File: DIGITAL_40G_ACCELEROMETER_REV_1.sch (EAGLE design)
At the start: 26 parts, among them IC1 ADIS16500AMLZ, IC2 LTC6820IUD#PBF, IC3 LDL1117S33R, T1 782482_33VC

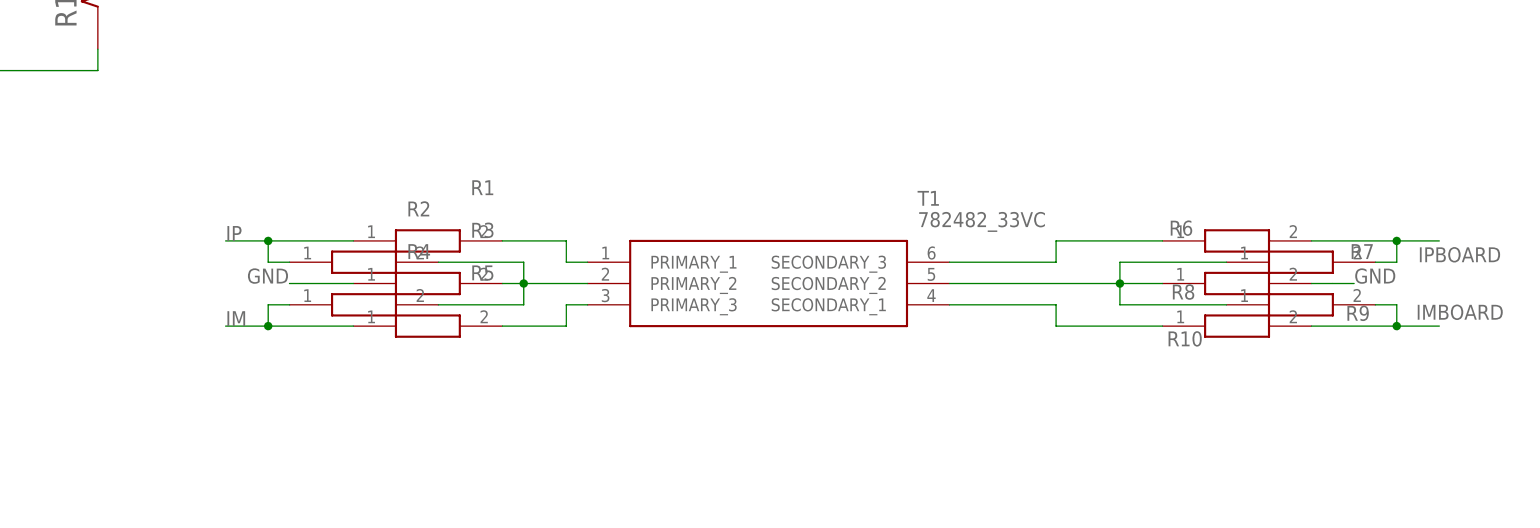
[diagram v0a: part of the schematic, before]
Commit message: Completed First Draft of Digital 40G Board Layout
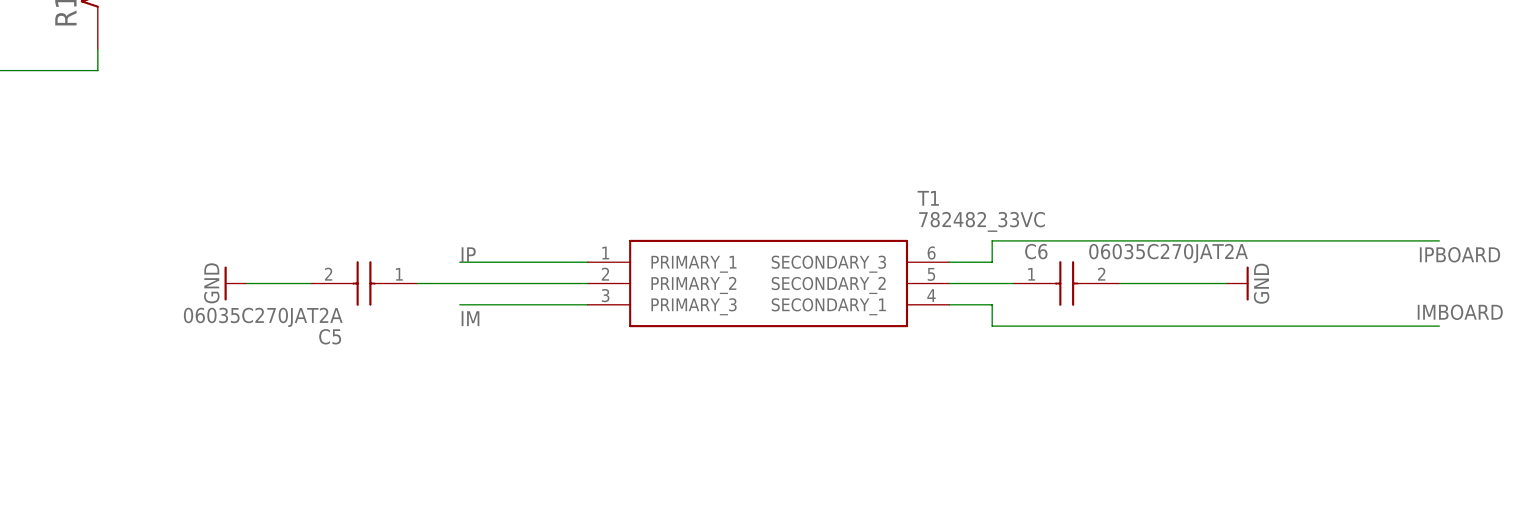
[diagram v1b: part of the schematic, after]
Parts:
- removed R1, R10, R2, R3, R4, R5, R6, R7, R8, R9: CRG0402ZR, CRG0402ZR:CRG0402ZR
- added C5, C6: 06035C270JAT2A, SamacSys_Parts:06035C270JAT2A
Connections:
- removed net N$10: R7.1, R8.1, R9.1, T1.SECONDARY_2
- removed net N$5: R2.2, R3.2, R4.2, T1.PRIMARY_2
- removed net N$6: R5.2, T1.PRIMARY_3
- removed net N$7: R1.2, T1.PRIMARY_1
- removed net N$8: R6.1, T1.SECONDARY_3
- removed net N$9: R10.1, T1.SECONDARY_1
- new net N$1: C6.1, T1.SECONDARY_2
- new net N$2: C5.1, T1.PRIMARY_2
- net GND: now also C5.2, C6.2; no longer R3.1, R8.2
- net IM: now also T1.PRIMARY_3; no longer R4.1, R5.1
- net IMBOARD: now also T1.SECONDARY_1; no longer R10.2, R9.2
- net IP: now also T1.PRIMARY_1; no longer R1.1, R2.1
- net IPBOARD: now also T1.SECONDARY_3; no longer R6.2, R7.2

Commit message: Second Draft of Digital 40G Layout. Ready for review.
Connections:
- net DR: now also Z1.2; no longer Z1.4
- net IM: now also Z1.3; no longer Z1.2
- net IP: now also Z1.4; no longer Z1.3
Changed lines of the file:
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@@
 <wire x1="165.1" y1="104.14" x2="165.1" y2="93.98" width="0.1524" layer="91"/>
 <label x="165.1" y="106.68" size="1.778" layer="95" rot="R180"/>
+<junction x="165.1" y="104.14"/>
 </segment>
 </net>
@@
 </segment>
 <segment>
+<pinref part="Z1" gate="Z$1" pin="2"/>
+<wire x1="299.72" y1="116.84" x2="299.72" y2="109.22" width="0.1524" layer="91"/>
+<label x="299.72" y="109.22" size="1.778" layer="95"/>
+</segment>
+</net>
+<net name="IP" class="0">
+<segment>
+<pinref part="T1" gate="G$1" pin="PRIMARY_1"/>
+<wire x1="292.1" y1="50.8" x2="276.86" y2="50.8" width="0.1524" layer="91"/>
+<label x="276.86" y="50.8" size="1.778" layer="95"/>
+</segment>
+<segment>
 <pinref part="Z1" gate="Z$1" pin="4"/>
-<wire x1="281.94" y1="129.54" x2="274.32" y2="129.54" width="0.1524" layer="91"/>
-<label x="274.32" y="132.08" size="1.778" layer="95"/>
-</segment>
-</net>
-<net name="IP" class="0">
+<wire x1="281.94" y1="129.54" x2="271.78" y2="129.54" width="0.1524" layer="91"/>
+<label x="271.78" y="129.54" size="1.778" layer="95"/>
+</segment>
+</net>
+<net name="IM" class="0">
+<segment>
+<pinref part="T1" gate="G$1" pin="PRIMARY_3"/>
+<wire x1="292.1" y1="45.72" x2="276.86" y2="45.72" width="0.1524" layer="91"/>
+<label x="276.86" y="43.18" size="1.778" layer="95"/>
+</segment>
 <segment>
 <pinref part="Z1" gate="Z$1" pin="3"/>
@@
 <label x="287.02" y="109.22" size="1.778" layer="95"/>
 </segment>
-<segment>
-<pinref part="T1" gate="G$1" pin="PRIMARY_1"/>
-<wire x1="292.1" y1="50.8" x2="276.86" y2="50.8" width="0.1524" layer="91"/>
-<label x="276.86" y="50.8" size="1.778" layer="95"/>
-</segment>
-</net>
-<net name="IM" class="0">
-<segment>
-<pinref part="Z1" gate="Z$1" pin="2"/>
-<wire x1="299.72" y1="116.84" x2="299.72" y2="109.22" width="0.1524" layer="91"/>
-<label x="299.72" y="109.22" size="1.778" layer="95"/>
-</segment>
-<segment>
-<pinref part="T1" gate="G$1" pin="PRIMARY_3"/>
-<wire x1="292.1" y1="45.72" x2="276.86" y2="45.72" width="0.1524" layer="91"/>
-<label x="276.86" y="43.18" size="1.778" layer="95"/>
-</segment>
-</net>
+</net>

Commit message: Final Board Layout Update. Incorporated new connector model.
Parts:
- R11: device TNPW0402100RBYEP:TNPW0402100RBYEP -> SamacSys_Parts:TNPW0402100RBYEP
- R16, R17: device CRG0402ZR:CRG0402ZR -> SamacSys_Parts:CRG0402ZR
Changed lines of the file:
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@@
 <part name="GND15" library="supply1" library_urn="urn:adsk.eagle:library:371" deviceset="GND" device=""/>
 <part name="GND16" library="supply1" library_urn="urn:adsk.eagle:library:371" deviceset="GND" device=""/>
-<part name="Z1" library="SamacSys_Parts" library_urn="urn:adsk.eagle:library:31941355" deviceset="AS_FEMALE_5_PIN" device="" package3d_urn="urn:adsk.eagle:package:34263750/6"/>
+<part name="Z1" library="SamacSys_Parts" library_urn="urn:adsk.eagle:library:31941355" deviceset="AS_FEMALE_5_PIN" device="" package3d_urn="urn:adsk.eagle:package:34263750/8"/>
 <part name="T1" library="SamacSys_Parts" library_urn="urn:adsk.eagle:library:34029941" deviceset="782482_33VC" device="" package3d_urn="urn:adsk.eagle:package:34608653/2"/>
 <part name="IC3" library="SamacSys_Parts" library_urn="urn:adsk.eagle:library:31941355" deviceset="LDL1117S33R" device="" package3d_urn="urn:adsk.eagle:package:34485302/2"/>
@@
 <part name="C3" library="SamacSys_Parts" library_urn="urn:adsk.eagle:library:34029941" deviceset="JMK107BB7475KA-T" device="" package3d_urn="urn:adsk.eagle:package:34029965/6"/>
 <part name="GND19" library="supply1" library_urn="urn:adsk.eagle:library:371" deviceset="GND" device=""/>
-<part name="R11" library="TNPW0402100RBYEP" deviceset="TNPW0402100RBYEP" device="" value="100"/>
+<part name="R11" library="SamacSys_Parts" library_urn="urn:adsk.eagle:library:34029941" deviceset="TNPW0402100RBYEP" device="" package3d_urn="urn:adsk.eagle:package:34740186/6" value="100"/>
 <part name="R12" library="SamacSys_Parts" library_urn="urn:adsk.eagle:library:34029941" deviceset="CPF0402B1K21E1" device="" package3d_urn="urn:adsk.eagle:package:34746415/2"/>
 <part name="R13" library="SamacSys_Parts" library_urn="urn:adsk.eagle:library:34029941" deviceset="CPF0402B1K21E1" device="" package3d_urn="urn:adsk.eagle:package:34746415/2"/>
@@
 <part name="R15" library="SamacSys_Parts" library_urn="urn:adsk.eagle:library:34029941" deviceset="ERA-2AEB7870X" device="" package3d_urn="urn:adsk.eagle:package:34746584/2"/>
 <part name="C4" library="SamacSys_Parts" library_urn="urn:adsk.eagle:library:34029941" deviceset="C0402C103J5RECAUTO" device="" package3d_urn="urn:adsk.eagle:package:34744484/2"/>
-<part name="R16" library="CRG0402ZR" deviceset="CRG0402ZR" device=""/>
-<part name="R17" library="CRG0402ZR" deviceset="CRG0402ZR" device=""/>
+<part name="R16" library="SamacSys_Parts" library_urn="urn:adsk.eagle:library:34029941" deviceset="CRG0402ZR" device="" package3d_urn="urn:adsk.eagle:package:34740186/6"/>
+<part name="R17" library="SamacSys_Parts" library_urn="urn:adsk.eagle:library:34029941" deviceset="CRG0402ZR" device="" package3d_urn="urn:adsk.eagle:package:34740186/6"/>
 <part name="C5" library="SamacSys_Parts" library_urn="urn:adsk.eagle:library:34029941" deviceset="06035C270JAT2A" device="" package3d_urn="urn:adsk.eagle:package:34029965/6"/>
 <part name="C6" library="SamacSys_Parts" library_urn="urn:adsk.eagle:library:34029941" deviceset="06035C270JAT2A" device="" package3d_urn="urn:adsk.eagle:package:34029965/6"/>
